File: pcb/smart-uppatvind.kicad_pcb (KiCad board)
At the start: 4 copper layers, 76 x 36 mm, 63 parts, among them J1 PWR, J2 EXT_SENSOR, J3 UART_PROG, J4 FAN, Q1 IRLML9301, Q2 MMBT3904, Q3 MMBT3904, Q4 MMBT3904, Q5 Q_NMOS_GSD, SW1 EN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

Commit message: Adjusted layout
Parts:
- C11, R6: moved to B.Cu
- moved C3 25.2 mm to (102.8, 67.7), turned to -90 degrees
- moved U1 21.4 mm to (96.8, 65.7), turned to 0 degrees
- moved C2 21.4 mm to (90.8, 67.7), turned to 90 degrees
- moved R15 12.5 mm to (83.6, 62.5)
- moved R18 12.5 mm to (83.6, 64.7)
- moved R14 9.78 mm to (79.3, 62.5), turned to 180 degrees
- moved Q3 9.53 mm to (83.7, 67.7), turned to 0 degrees
- moved Q1 7.70 mm to (79.4, 67.7), turned to 0 degrees
- moved C9 6.26 mm to (79.1, 48.5), turned to 180 degrees
- moved R11 5.94 mm to (79.3, 64.7), turned to 0 degrees
- moved R6 3.52 mm to (79.1, 48.5), turned to 0 degrees
- moved Q5 2.88 mm to (92.2, 74.2)
- moved R21 2.75 mm to (92.1, 71.2)
- moved R24 2.75 mm to (96.3, 72.7)
- moved R25 2.75 mm to (96.3, 75.0)
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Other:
- board size 76 x 36 mm -> 74 x 36 mm

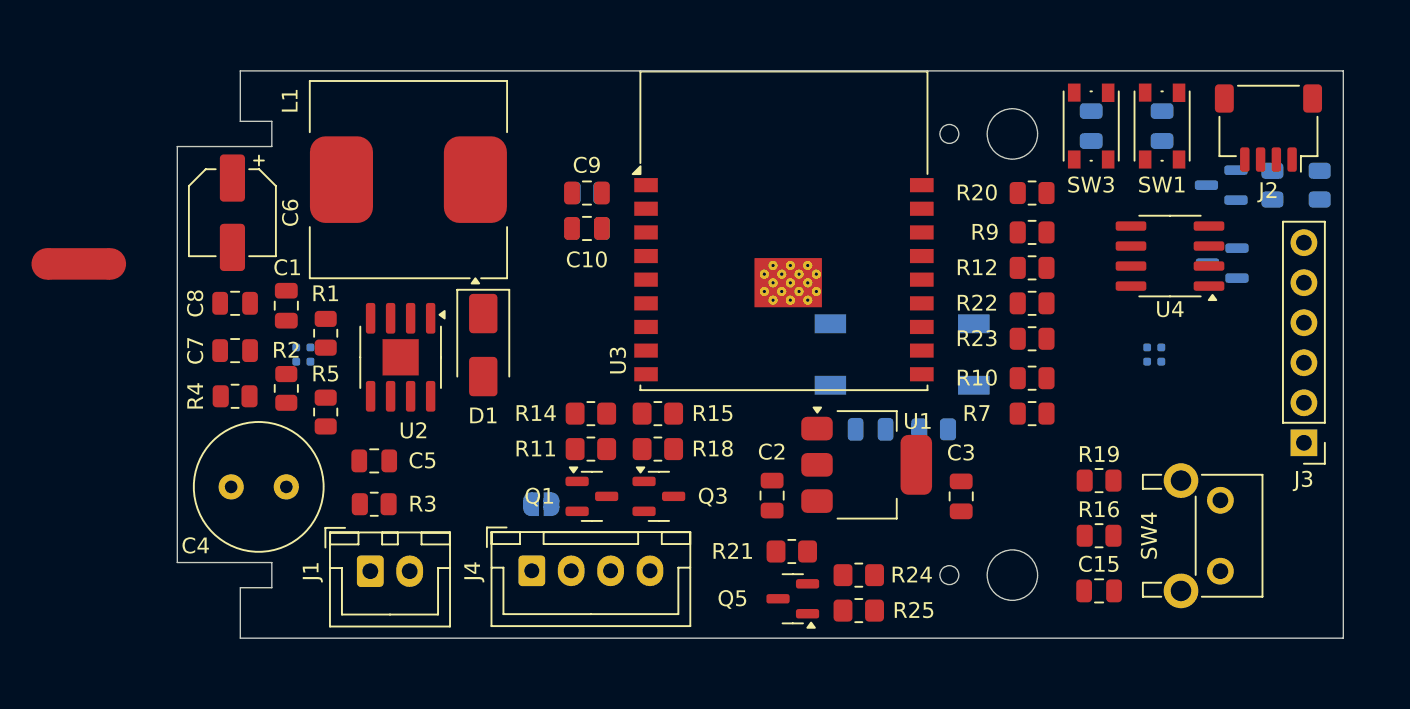
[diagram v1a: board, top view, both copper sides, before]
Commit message: Partly routed power management
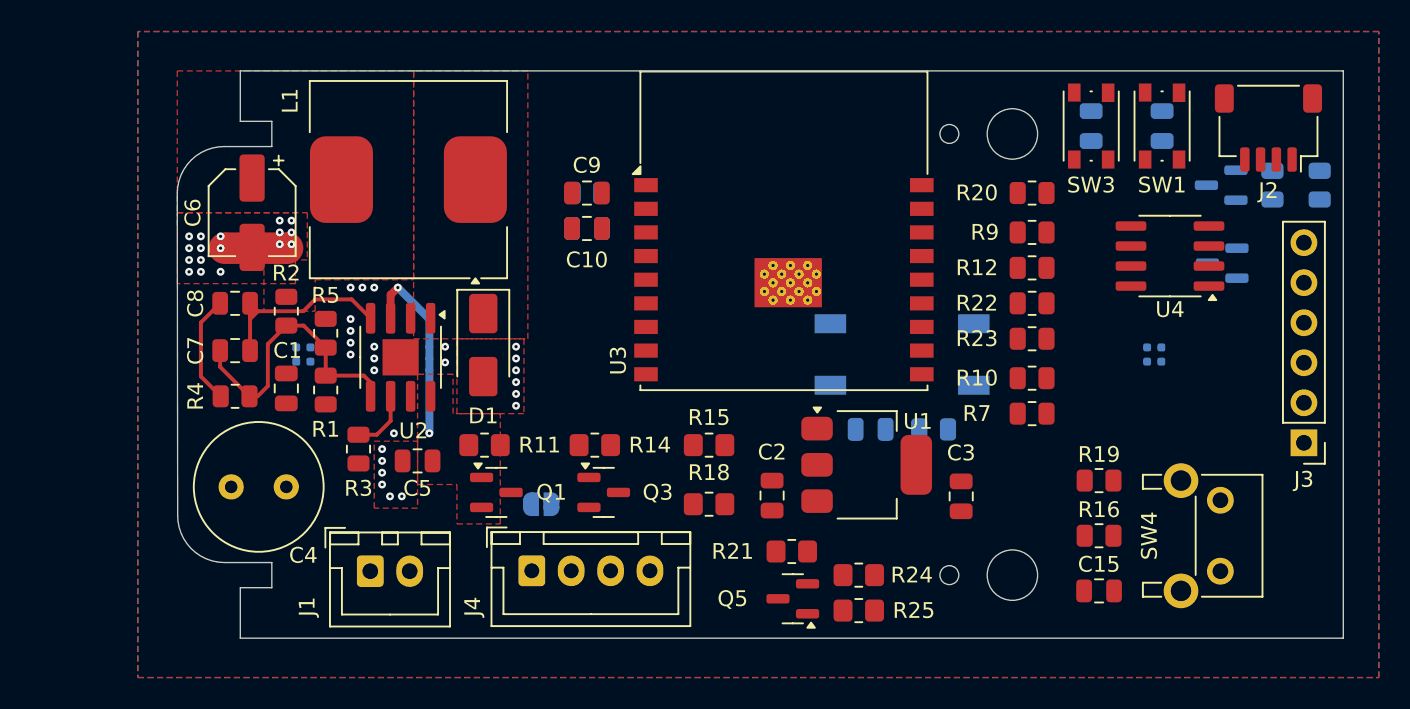
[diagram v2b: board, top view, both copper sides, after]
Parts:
- moved NT1 11.3 mm to (58.1, 52.0)
- moved R11 6.75 mm to (72.6, 64.5)
- moved Q1 6.07 mm to (73.3, 67.5)
- moved C1 5.25 mm to (60.0, 60.9)
- moved R5 5.00 mm to (62.5, 57.4), turned to -90 degrees
- moved R2 4.90 mm to (60.0, 56.0)
- moved R18 4.78 mm to (86.8, 68.2)
- moved R15 3.82 mm to (86.8, 64.5)
- moved R3 3.64 mm to (64.6, 64.7), turned to 90 degrees
- moved R1 3.60 mm to (62.5, 61.0), turned to -90 degrees
- moved Q3 3.51 mm to (80.2, 67.5)
- moved C5 2.75 mm to (68.3, 65.5), turned to 180 degrees
- moved R14 2.02 mm to (79.6, 64.5), turned to 0 degrees
- moved C6 1.25 mm to (57.9, 49.7)
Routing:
- net Net-(U2-FB): track 0.00 -> 18.2 mm
- net Net-(U2-COMP): track 0.00 -> 12.7 mm
- net +24V: track 0.00 -> 12.2 mm, vias 0 -> 2
- net Net-(C8-Pad2): track 0.00 -> 6.93 mm
- net Net-(U2-FSW): track 0.00 -> 3.96 mm
- net GNDPWR: vias 0 -> 23
- net GND: vias 0 -> 19
- added copper zone on F.Cu, net +24V
- added copper zone on In1.Cu, net +24V
- added copper zone on F.Cu, net +5V
- added copper zone on B.Cu, net GND
- added copper zone on F.Cu, net GND
- added copper zone on In2.Cu, net GND
- added copper zone on F.Cu, net GNDPWR
- added copper zone on In2.Cu, net GNDPWR
- added copper zone on F.Cu, net Net-(D1-K)
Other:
- outline, holes or cut-outs redrawn

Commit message: Adjusted MCU pin assignment, progressed with power routing
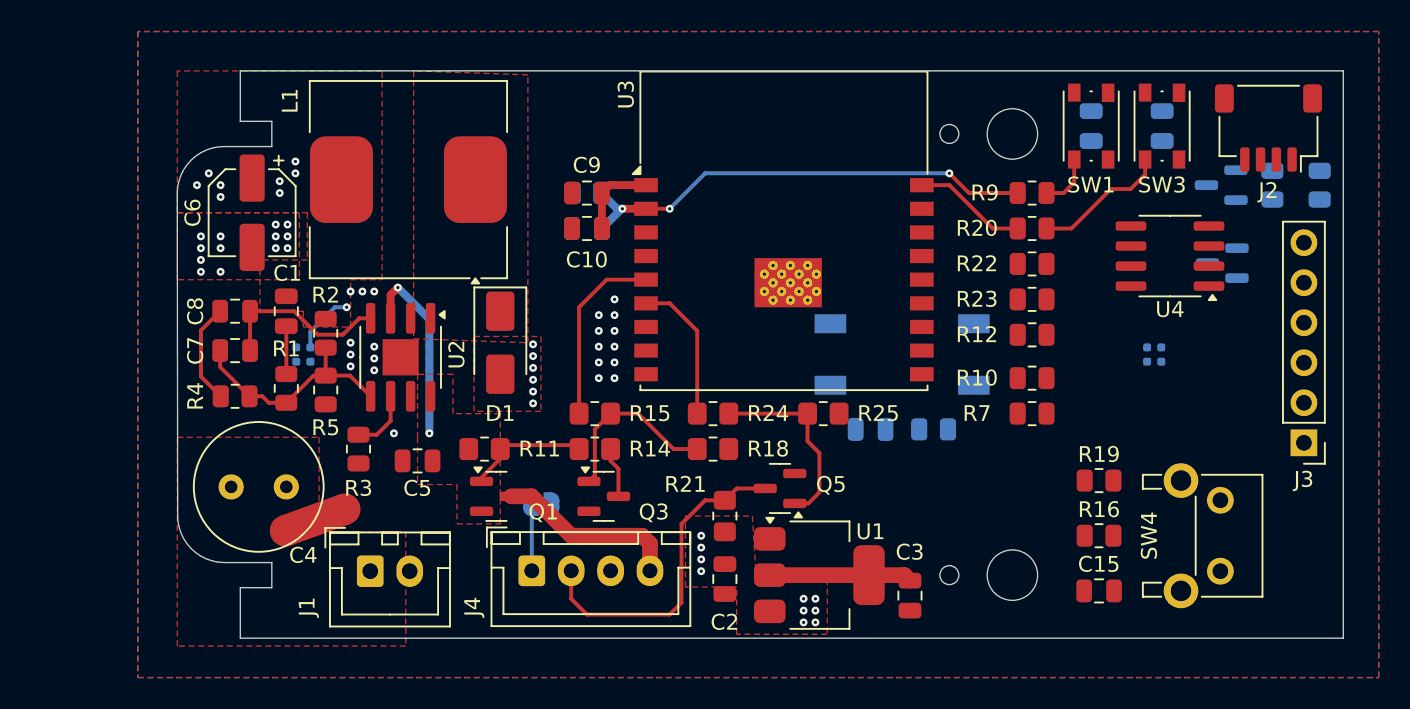
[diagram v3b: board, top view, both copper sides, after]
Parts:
- moved NT1 17.7 mm to (61.9, 69.2), turned to 20 degrees
- moved R24 13.8 mm to (87.1, 62.5), turned to 180 degrees
- moved R25 12.7 mm to (94.1, 62.5)
- moved U1 7.62 mm to (93.8, 72.7)
- moved R15 7.52 mm to (79.6, 62.5), turned to 180 degrees
- moved C3 7.09 mm to (99.6, 74.0)
- moved Q5 7.05 mm to (91.3, 67.2)
- moved C2 6.09 mm to (87.8, 73.0), turned to -90 degrees
- moved C1 4.90 mm to (60.0, 56.0)
- moved R21 4.81 mm to (87.8, 69.0), turned to 90 degrees
- moved C13 4.50 mm to (111.1, 44.2)
- moved C14 4.50 mm to (115.6, 44.2)
- moved SW1 4.50 mm to (111.1, 44.2)
- moved SW3 4.50 mm to (115.6, 44.2)
- moved R12 4.25 mm to (107.3, 57.5)
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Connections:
- C5 pad 2: GNDPWR -> GND
- U3 pad 10: /FAN_EN -> Net-(JP1-B)
- U3 pad 16: /PWM -> /SCL
- U3 pad 17: Net-(JP1-B) -> /SDA
- U3 pad 5: /SDA -> /FAN_EN
- U3 pad 6: /SCL -> /PWM
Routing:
- net /EN: track 0.00 -> 30.1 mm, vias 0 -> 3
- net /PWM_5V: track 0.00 -> 20.7 mm
- net VDD: track 0.00 -> 14.3 mm
- net Net-(Q5-G): track 0.00 -> 12.2 mm
- net /FAN_24V: track 0.00 -> 11.8 mm
- net /FAN_EN: track 0.00 -> 11.5 mm
- net Net-(Q3-B): track 0.00 -> 11.3 mm
- net /PWM: track 0.00 -> 9.22 mm
- net Net-(Q4-C): track 0.00 -> 8.63 mm
- net Net-(Q1-G): track 0.00 -> 7.54 mm
- net /BOOT: track 0.00 -> 7.23 mm
- net /FG: track 0.00 -> 4.25 mm
- net +5V: track 0.00 -> 3.94 mm, vias 0 -> 19
- net Net-(U2-FB): track 18.2 -> 14.6 mm
- net Net-(Q2-C): track 0.00 -> 3.49 mm
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- added copper zone on In1.Cu, net +5V
- added copper zone on In1.Cu, net VDD

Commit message: Adjusted layout
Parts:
- C11, Q2, Q4, R13, R17, R6: moved to F.Cu
- C15: moved to B.Cu
- moved C11 32.0 mm to (111.1, 50.5), turned to 0 degrees
- moved R6 28.3 mm to (107.3, 50.5)
- moved U4 19.3 mm to (102.8, 66.5), turned to 0 degrees
- moved R22 17.3 mm to (110.6, 70.0)
- moved R23 13.2 mm to (110.6, 68.0)
- moved C12 9.50 mm to (97.1, 54.0), turned to 0 degrees
- moved R8 9.50 mm to (101.1, 54.0), turned to 0 degrees
- moved R16 8.52 mm to (111.0, 61.7), turned to 180 degrees
- moved R17 7.79 mm to (120.8, 55.5), turned to 90 degrees
- moved R19 6.56 mm to (107.3, 61.7), turned to 180 degrees
- moved R13 6.21 mm to (120.8, 52.0)
- moved C15 5.32 mm to (115.6, 70.2), turned to 90 degrees
- moved Q4 4.04 mm to (117.8, 51.7), turned to 90 degrees
- moved Q2 3.21 mm to (117.8, 55.7), turned to -90 degrees
- moved R10 3.00 mm to (107.3, 57.2)
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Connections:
- U3 pad 10: Net-(JP1-B) -> /SW_FILTER
- U3 pad 3: /SW_FILTER -> Net-(JP1-B)
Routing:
- net /TX: track 0.00 -> 18.6 mm
- net /RX: track 0.00 -> 16.9 mm
- net Net-(Q2-C): track 3.49 -> 12.1 mm, vias 0 -> 1
- net /SW_MAIN: track 0.00 -> 7.12 mm
- net Net-(U3-IO20/RXD): track 0.00 -> 6.50 mm
- net Net-(U3-IO21/TXD): track 0.00 -> 6.19 mm
- net /FG: track 4.25 -> 0.00 mm
- net /PWM_5V: track 20.7 -> 23.9 mm
- net VDD: track 14.3 -> 11.2 mm, vias 0 -> 11
- net Net-(Q5-G): track 12.2 -> 10.5 mm
- net /BOOT: track 7.23 -> 8.15 mm
- net Net-(Q4-C): track 8.63 -> 8.80 mm, vias 0 -> 1
- net /EN: track 30.1 -> 30.3 mm, vias 3 -> 2
- added copper zone on F.Cu, net VDD

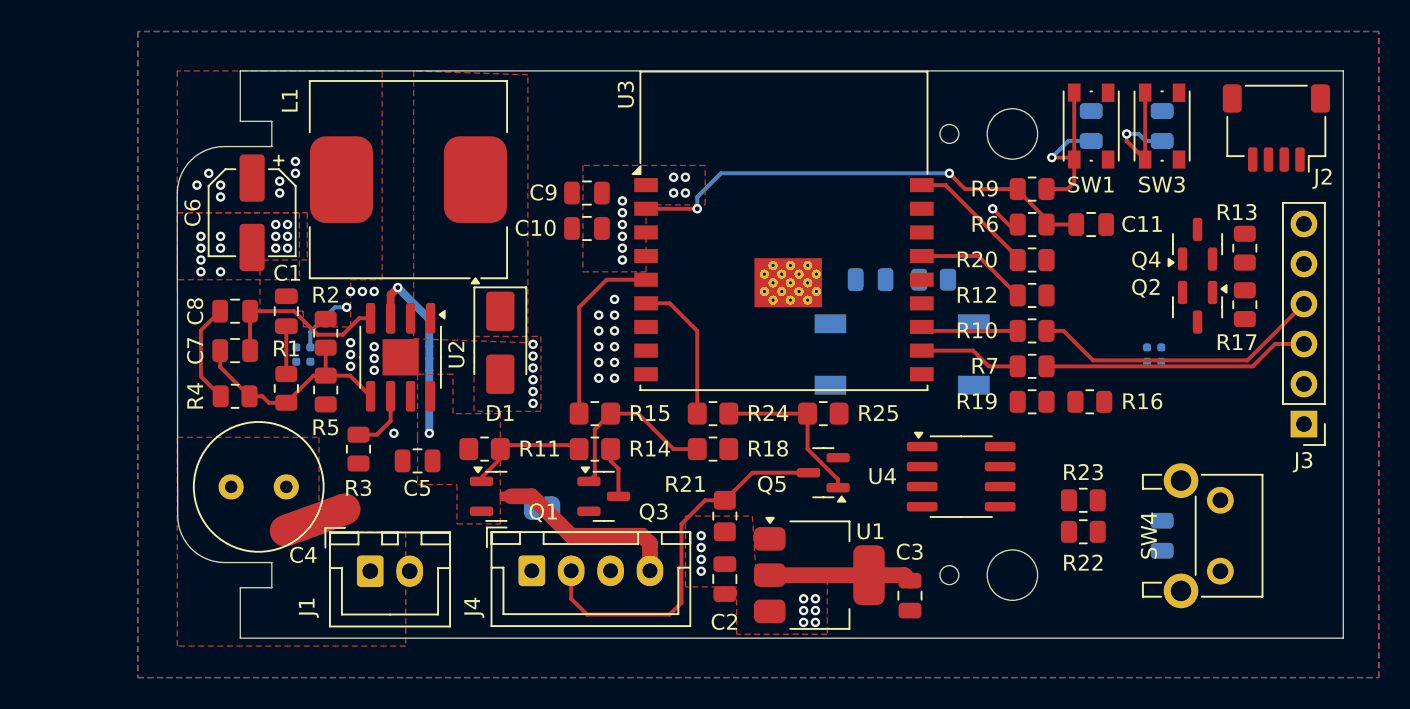
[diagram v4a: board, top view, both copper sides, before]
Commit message: Added logos
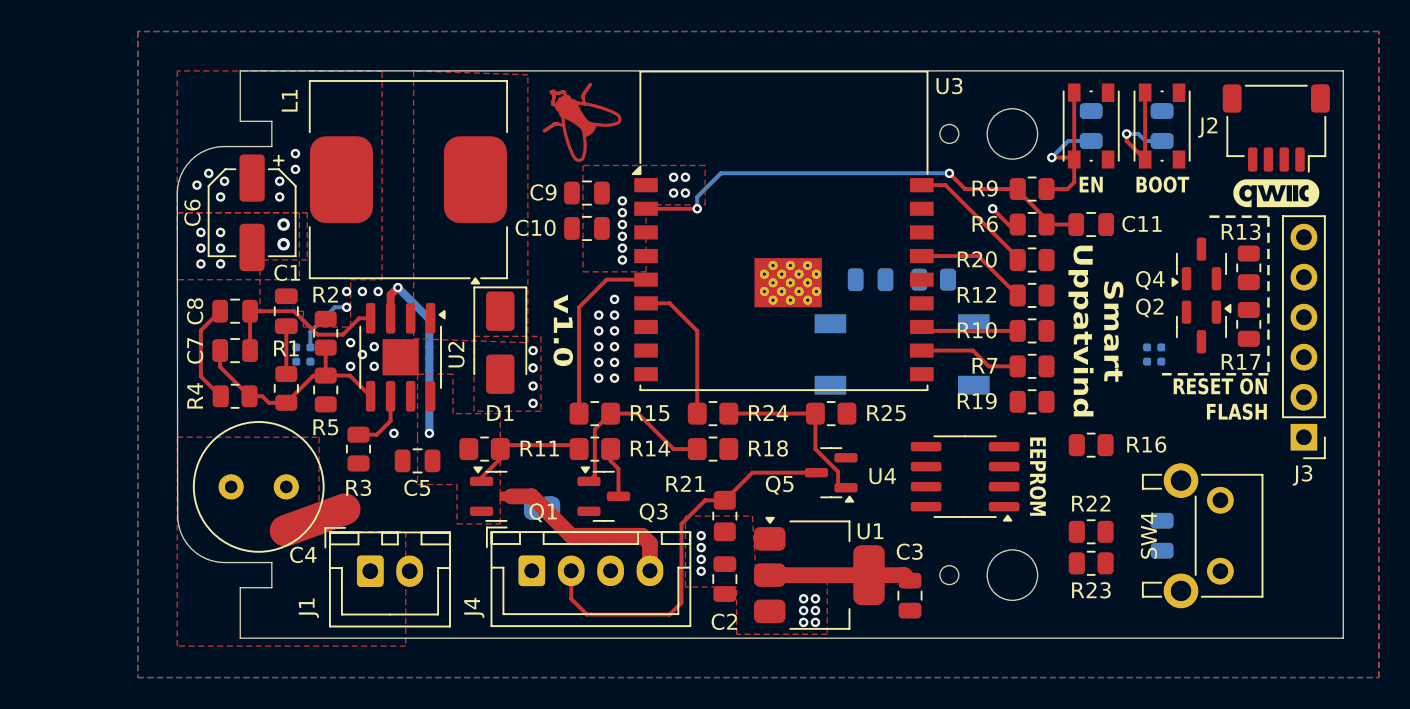
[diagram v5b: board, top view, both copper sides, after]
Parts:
- added G***: LOGO, SparkFun-Qwiic:qwiic_5.5mm, F.Cu at (122.8, 48.5)
- added REF**: Logo_Moucha_4.5x4.5mm_Copper, Moucha_Graphics:Logo_Moucha_4.5x4.5mm_Copper, F.Cu at (78.6, 43.7)
- moved R23 4.03 mm to (111.1, 72.0)
- moved R16 2.75 mm to (111.1, 64.5)
- moved Q2 1.27 mm to (118.1, 57.0)
- moved Q4 1.27 mm to (118.1, 53.0)
- moved R13 1.27 mm to (121.1, 53.2)
- moved R17 1.27 mm to (121.1, 56.8)
- moved J3 0.84 mm to (124.6, 64.0)
- moved Q5 0.50 mm to (94.6, 66.2)
- moved R22 0.50 mm to (111.1, 70.0)
- moved R25 0.50 mm to (94.6, 62.5)
- moved U4 0.25 mm to (103.1, 66.5), turned to 180 degrees
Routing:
- net /TX: track 18.6 -> 0.00 mm
- net /RX: track 16.9 -> 0.00 mm
- net /PWM_5V: track 23.9 -> 24.4 mm
- net GNDPWR: vias 19 -> 12
- net GND: vias 21 -> 20
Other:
- board text added: "BOOT"
- board text added: "EEPROM"
- board text added: "EN"
- board text added: "RESET ON FLASH"
- board text added: "Smart Uppatvind"
- board text added: "v${REVISION}"

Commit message: Routed all signals, added connector pinout labels
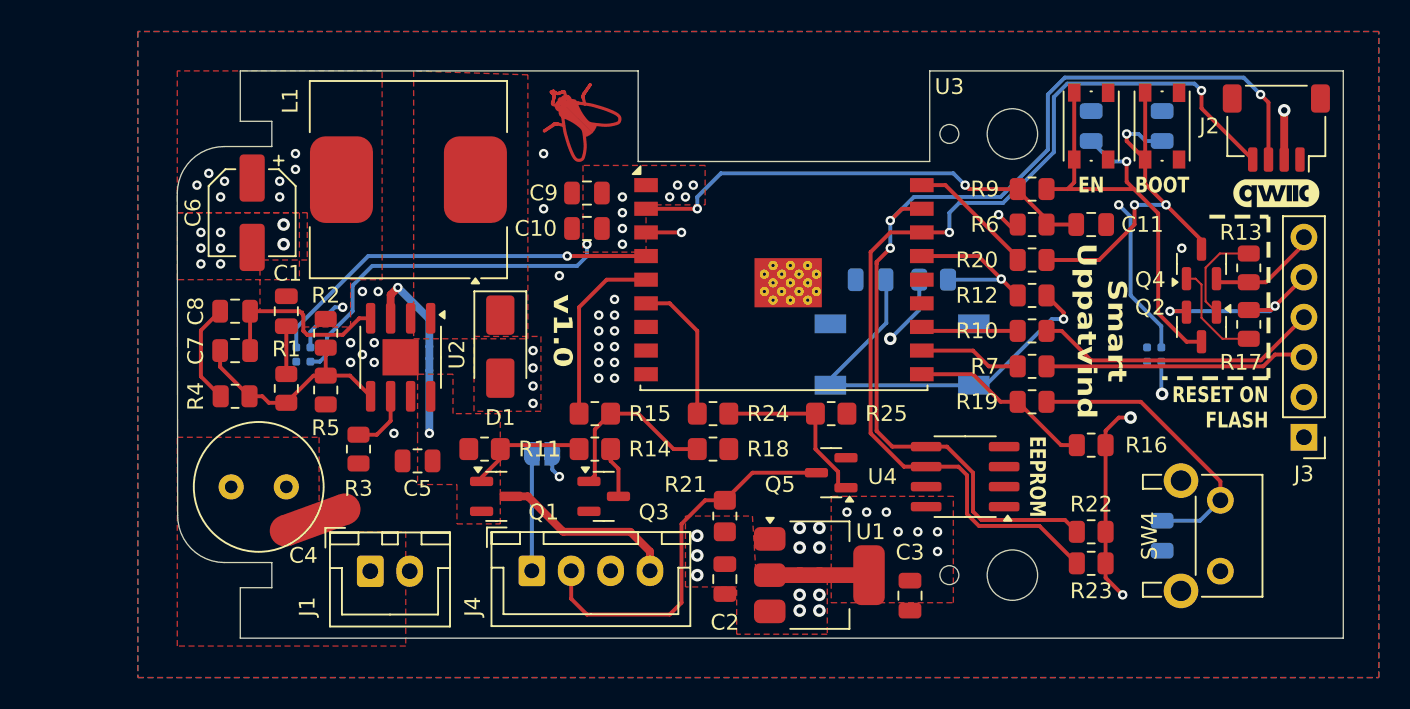
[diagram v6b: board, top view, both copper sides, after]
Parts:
- moved D2 54.0 mm to (61.1, 58.7), turned to 180 degrees
- moved D3 54.0 mm to (115.1, 58.7), turned to 90 degrees
- moved JP1 3.45 mm to (76.2, 65.0)
- moved D1 0.25 mm to (73.6, 58.2)
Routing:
- net Net-(D2-DOUT): track 0.00 -> 70.6 mm, vias 0 -> 2
- net /SDA: track 0.00 -> 66.9 mm, vias 0 -> 3
- net /SCL: track 0.00 -> 63.6 mm, vias 0 -> 2
- net +5V: track 3.94 -> 39.7 mm, vias 19 -> 17
- net Net-(C12-Pad2): track 0.00 -> 26.7 mm, vias 0 -> 1
- net /LED: track 0.00 -> 25.3 mm, vias 0 -> 1
- net Net-(JP1-B): track 0.00 -> 24.8 mm, vias 0 -> 2
- net Net-(C15-Pad2): track 0.00 -> 18.6 mm
- net /TX: track 0.00 -> 18.2 mm
- net VDD: track 11.2 -> 28.3 mm, vias 11 -> 20
- net Net-(Q4-C): track 8.80 -> 25.7 mm, vias 1 -> 3
- net /RX: track 0.00 -> 16.7 mm
- net Net-(Q2-C): track 12.1 -> 28.6 mm
- net /RTS: track 0.00 -> 12.2 mm, vias 0 -> 2
- net /SW_FILTER: track 0.00 -> 11.7 mm
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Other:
- outline, holes or cut-outs redrawn
- board text added: "24V"
- board text added: "DTR"
- board text added: "FG"
- board text added: "FG → IO4"
- board text added: "GND"
- board text added: "PWM"
- board text added: "RTS"
- board text added: "RX"
- board text added: "SCL"
- board text added: "SDA"
- board text added: "TX"
- board text added: "VDD"
